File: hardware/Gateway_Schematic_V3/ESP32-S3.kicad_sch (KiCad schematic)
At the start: 13 parts, among them J6 Conn_01x07_Pin, SW1 SW_Push, SW2 SW_Push, U1 ESP32-S3-WROOM-1

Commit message: Update PCB Layout for Gateway (24/3/2026)
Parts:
- added CLK0, CS0, MISO0, MOSI0, TP2, TP3: ~, IVS_NEW_FOOTPRINT:TestPoint_throughtHole_D1.0mm, symbol Connector:TestPoint
- added ESP_RX1, ESP_SCL0, ESP_SDA0, ESP_TX1: TestPoint, IVS_NEW_FOOTPRINT:TestPoint_throughtHole_D1.0mm, symbol Connector:TestPoint
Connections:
- net ESP.SCL: now also ESP_SCL0.1
- net ESP.SDA: now also ESP_SDA0.1
- net ESP_ETH.CLK: now also CLK0.1
- net ESP_ETH.MISO: now also MISO0.1
- net ESP_ETH.MOSI: now also MOSI0.1
- net ESP_ETH_CS: now also CS0.1
- net ESP_HMI_RX: now also ESP_RX1.1
- net ESP_HMI_TX: now also ESP_TX1.1
- net UART1_RX: now also TP3.1
- net UART1_TX: now also TP2.1

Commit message: feat: Second review
Thay đổi kích thước chữ từ 1mm thành 0.8mm của các linh kiện - resize 1mm text size to 0.8mm
change direction of text footprint across placement direction
Note: Nhớ thay đổi footprint của nút nhấn
Thay đổi vị trí chữ để không bị chồng lấn với via
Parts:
- SW1, SW2: footprint IVS_FOOTPRINTS:SW_SPST_PTS810 -> Button_Switch_SMD:SW_SPST_B3U-1000P
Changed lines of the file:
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@@
 			)
 		)
-		(property "Footprint" "IVS_FOOTPRINTS:SW_SPST_PTS810"
+		(property "Footprint" "Button_Switch_SMD:SW_SPST_B3U-1000P"
 			(at 68.58 69.85 0)
 			(effects
@@
 			)
 		)
-		(property "Footprint" "IVS_FOOTPRINTS:SW_SPST_PTS810"
+		(property "Footprint" "Button_Switch_SMD:SW_SPST_B3U-1000P"
 			(at 67.31 69.85 0)
 			(effects

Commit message: Update PCB Layout for Gateway: change button, add gnd vias, fix silkscreen
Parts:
- SW1, SW2: footprint Button_Switch_SMD:SW_SPST_B3U-1000P -> IVS_NEW_FOOTPRINT:SW_SPST_PTS810
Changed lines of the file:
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@@
 			)
 		)
-		(property "Footprint" "Button_Switch_SMD:SW_SPST_B3U-1000P"
+		(property "Footprint" "IVS_NEW_FOOTPRINT:SW_SPST_PTS810"
 			(at 68.58 69.85 0)
 			(effects
@@
 			)
 		)
-		(property "Footprint" "Button_Switch_SMD:SW_SPST_B3U-1000P"
+		(property "Footprint" "IVS_NEW_FOOTPRINT:SW_SPST_PTS810"
 			(at 67.31 69.85 0)
 			(effects

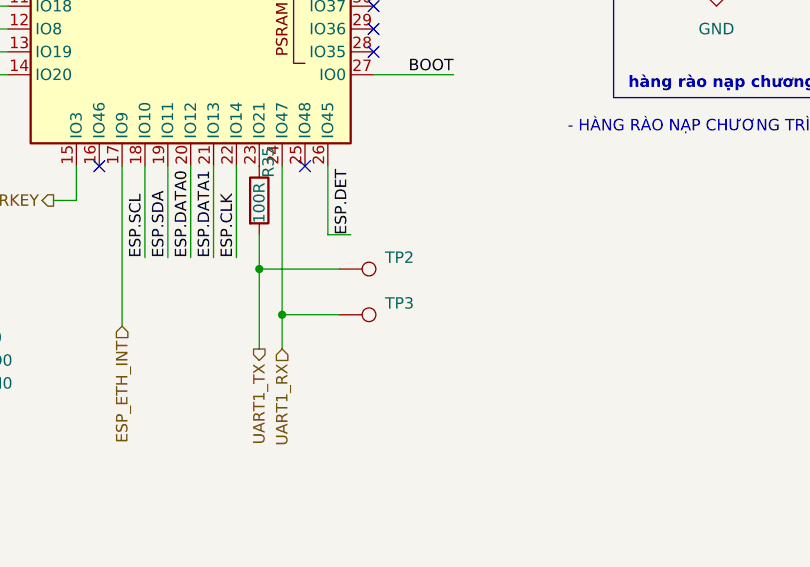
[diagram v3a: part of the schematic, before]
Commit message: Update Capacital for Shield of Ethernet
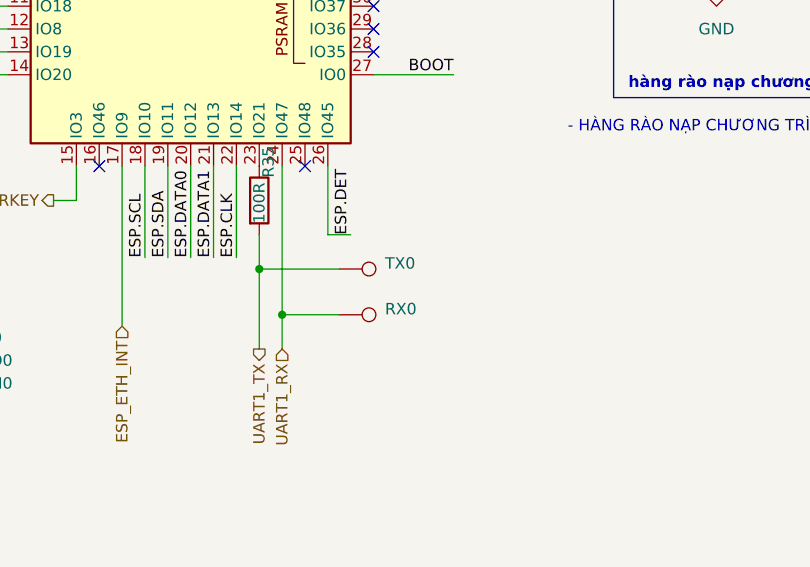
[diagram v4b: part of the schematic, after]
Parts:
- renumbered TP3 to RX0, TP2 to TX0
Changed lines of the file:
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@@
 		(dnp no)
 		(fields_autoplaced yes)
-		(property "Reference" "TP3"
-			(at 181.61 110.4899 90)
+		(property "Reference" "RX0"
+			(at 181.61 111.1249 90)
 			(effects
 				(font
@@
 		)
 		(property "Value" "~"
-			(at 181.61 113.0299 90)
+			(at 181.61 113.03 90)
 			(effects
 				(font
@@
 			(project "Schematic_V2_backup"
 				(path "/08b065f5-231d-43cb-bb9e-87dca43beac9/9fd5b551-28b1-42e9-a33d-c957f6949690"
-					(reference "TP3")
+					(reference "RX0")
 					(unit 1)
 				)
@@
 		(dnp no)
 		(fields_autoplaced yes)
-		(property "Reference" "TP2"
-			(at 181.61 105.4099 90)
+		(property "Reference" "TX0"
+			(at 181.61 106.0449 90)
 			(effects
 				(font
@@
 		)
 		(property "Value" "~"
-			(at 181.61 107.9499 90)
+			(at 181.61 107.95 90)
 			(effects
 				(font
@@
 			(project ""
 				(path "/08b065f5-231d-43cb-bb9e-87dca43beac9/9fd5b551-28b1-42e9-a33d-c957f6949690"
-					(reference "TP2")
+					(reference "TX0")
 					(unit 1)
 				)
